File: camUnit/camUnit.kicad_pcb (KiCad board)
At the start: 2 copper layers, 120 x 120 mm, 28 parts, among them J1 Conn_01x08, J2 Conn_01x04, J3 Conn_01x06, J4 Conn_01x06, J5 Conn_01x06, J6 Conn_01x06, SW1 SW_SPDT, SW2 ENC RST, SW3 SW_SPDT, U2 STM32F103Cx, Y1 8Mhz

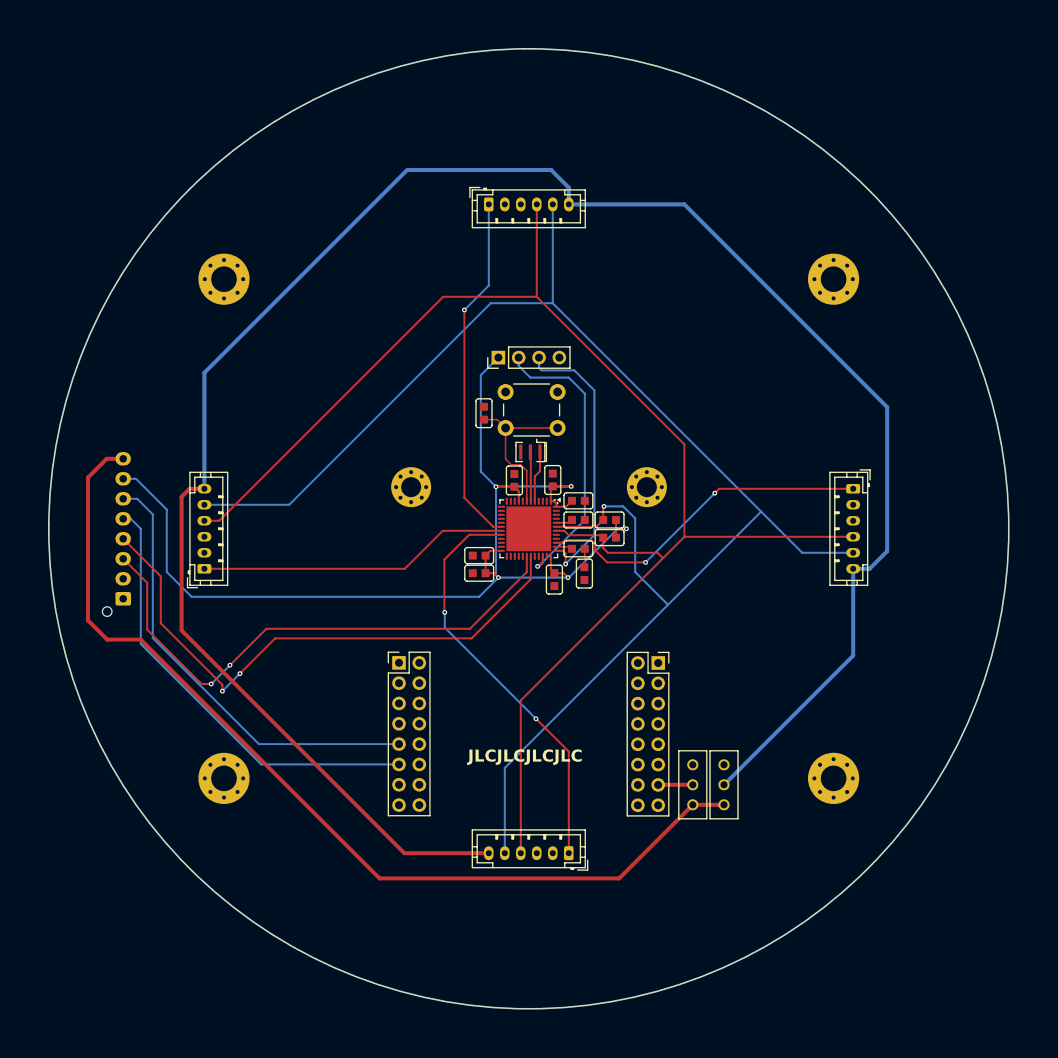
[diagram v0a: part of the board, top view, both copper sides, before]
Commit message: shrink pcb
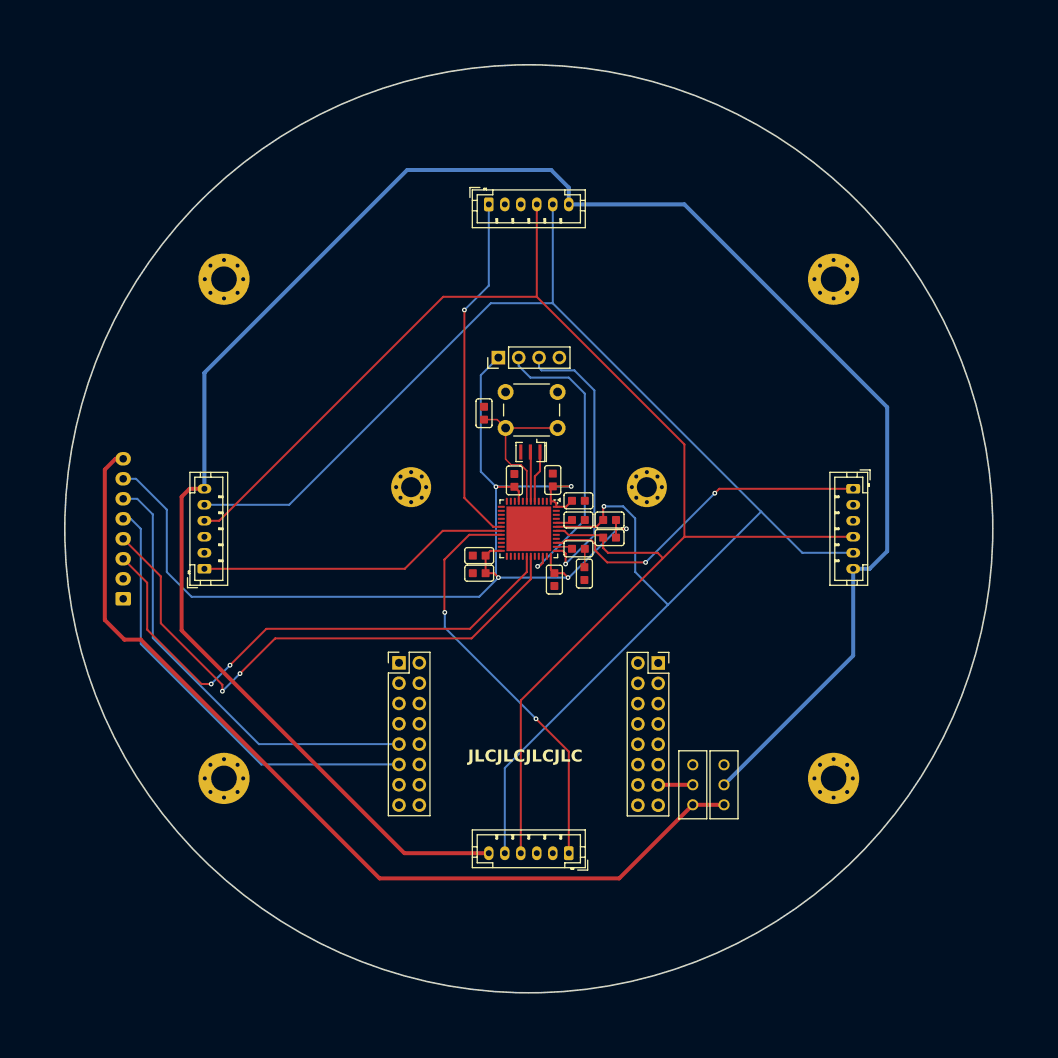
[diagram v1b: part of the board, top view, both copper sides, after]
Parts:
- J1: footprint Connector_JST:JST_XH_B8B-XH-AM_1x08_P2.50mm_Vertical -> Connector_JST:JST_XH_B8B-XH-A_1x08_P2.50mm_Vertical
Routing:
- net +5V FILT: track 119.9 -> 116.2 mm
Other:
- board size 120 x 120 mm -> 116 x 116 mm

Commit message: CamUnit
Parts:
- added C10: 2u2, Library:cap0603, F.Cu at (48.7, 115.3)
- added C11: 2u2, Library:cap0603, F.Cu at (48.7, 118.4)
- added C8: 2u2, Library:cap0603, F.Cu at (58.1, 107.1)
- added C9: 2u2, Library:cap0603, F.Cu at (64.6, 107.2)
- added FB1: 100R, Library:fb0805, F.Cu at (61.4, 106.5)
- added FB2: 100R, Library:fb0805, F.Cu at (53.6, 117.4)
- added Q1: IRLML6344TRPBF, Library:SOT95P237X112-3N, F.Cu at (157.7, 124.4)
- added Q2: IRLML6344TRPBF, Library:SOT95P237X112-3N, F.Cu at (161.7, 124.4)
- added R5: 1k, Library:res0603, F.Cu at (157.7, 127.8)
- added R6: 1k, Library:res0603, F.Cu at (157.7, 121.1)
- added R7: 1k, Library:res0603, F.Cu at (161.7, 127.8)
- added R8: 1k, Library:res0603, F.Cu at (161.7, 121.1)
- J1: moved to F.Cu
- moved J1 3.00 mm to (89.5, 110.1)
- moved SW3 0.09 mm to (161.7, 133.4), turned to -90 degrees
- turned SW1 to -90 degrees
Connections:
- SW1 pad 1: +5V FILT -> Net-(Q1-G)
- SW1 pad 2: /CAM PWR -> +3V3 FILT
- SW3 pad 1: +5V FILT -> Net-(Q2-G)
- SW3 pad 2: /TOF/TOF PWR -> +3V3 FILT
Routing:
- net +5V FILT: track 116.2 -> 141.8 mm
- net /CAM PWR: track 4.31 -> 15.1 mm
- net Net-(Q2-G): track 0.00 -> 5.61 mm
- net Net-(Q1-G): track 0.00 -> 5.61 mm
- net /TOF/TOF PWR: track 250.5 -> 247.1 mm, vias 0 -> 1
- net CAM TX: track 56.2 -> 54.0 mm
- net TOF TX: track 68.1 -> 66.2 mm
- net +3V3 FILT: track 141.5 -> 143.4 mm
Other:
- board size 116 x 116 mm -> 110 x 110 mm

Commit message: CamUnit
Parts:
- moved C11 58.9 mm to (101.1, 91.6), turned to 90 degrees
- moved C10 51.6 mm to (94.5, 91.6), turned to 90 degrees
- moved FB2 50.8 mm to (97.8, 92.3)
- moved C9 36.7 mm to (101.1, 111.2)
- moved FB1 36.6 mm to (97.8, 110.5)
- moved C8 36.6 mm to (94.5, 111.2)
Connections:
- J1 pad 7: +3V3 FILT -> +3V3
- J1 pad 8: +5V FILT -> +5V
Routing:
- net +3V3 FILT: track 143.4 -> 165.2 mm, vias 5 -> 7
- net /TOF/TOF PWR: track 247.1 -> 231.7 mm
- net +5V FILT: track 141.8 -> 131.1 mm, vias 0 -> 4
- net TOF RX: track 71.1 -> 73.0 mm, vias 2 -> 0
- net CAM RX: track 55.7 -> 53.8 mm
- net TOF TX: track 66.2 -> 66.3 mm, vias 2 -> 0
- added copper zone on F.Cu, net +3V3
- added copper zone on F.Cu, net +3V3 FILT
- added copper zone on F.Cu, net +5V
- added copper zone on F.Cu, net +5V FILT

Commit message: Fab
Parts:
- Y1: footprint Crystal:Resonator_SMD_Murata_CSTxExxV-3Pin_3.0x1.1mm -> Library:CSTCE8M00G52-R0
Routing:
- net /TOF/ENC OSC OUT: track 5.91 -> 6.68 mm
